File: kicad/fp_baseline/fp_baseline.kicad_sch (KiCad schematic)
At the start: 1 part, among them J1 JS220

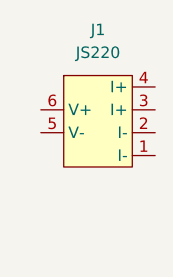
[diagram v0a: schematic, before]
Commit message: fix front copper polygon so it acts as prper copper pour around pads
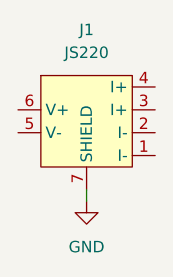
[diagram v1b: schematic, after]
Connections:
- new net GND: J1.7 (SHIELD)
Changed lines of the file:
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@@
 (kicad_sch (version 20211123) (generator eeschema)
   (paper "A4")
-  (symbol (lib_id "Joulescope:JS220") (at 140.97 100.33 0) (unit 1)
+  (wire (pts (xy 139.7 107.95) (xy 139.7 109.22))
+    (stroke (width 0) (type default) (color 0 0 0 0))
+  )
+  (symbol (lib_id "power:GND") (at 139.7 109.22 0) (unit 1)
     (in_bom yes) (on_board yes) (fields_autoplaced)
-    (property "Reference" "J1" (id 0) (at 140.97 90.17 0))
-    (property "Value" "JS220" (id 1) (at 140.97 92.71 0))
-    (property "Footprint" "Joulescope:JS220" (id 2) (at 140.97 100.33 0)
+    (property "Reference" "#PWR0101" (id 0) (at 139.7 115.57 0)
       (effects (font (size 1.27 1.27)) hide)
     )
-    (property "Datasheet" "" (id 3) (at 140.97 100.33 0)
+    (property "Value" "GND" (id 1) (at 139.7 114.3 0))
+    (property "Footprint" "" (id 2) (at 139.7 109.22 0)
+      (effects (font (size 1.27 1.27)) hide)
+    )
+    (property "Datasheet" "" (id 3) (at 139.7 109.22 0)
+      (effects (font (size 1.27 1.27)) hide)
+    )
+    (pin "1")
+  )
+  (symbol (lib_id "Joulescope:JS220") (at 139.7 100.33 0) (unit 1)
+    (in_bom yes) (on_board yes) (fields_autoplaced)
+    (property "Reference" "J1" (id 0) (at 139.7 90.17 0))
+    (property "Value" "JS220" (id 1) (at 139.7 92.71 0))
+    (property "Footprint" "Joulescope:JS220" (id 2) (at 139.7 100.33 0)
+      (effects (font (size 1.27 1.27)) hide)
+    )
+    (property "Datasheet" "" (id 3) (at 139.7 100.33 0)
       (effects (font (size 1.27 1.27)) hide)
     )
@@
     (pin "5")
     (pin "6")
+    (pin "7")
   )
   (sheet_instances
@@
   )
   (symbol_instances
+    (path "/371c245b-12ff-418c-ad6a-38bf35510b4d"
+      (reference "#PWR0101") (unit 1) (value "GND") (footprint "")
+    )
     (path "/376cee22-538a-400e-85e1-282bd8cf6c38"
       (reference "J1") (unit 1) (value "JS220") (footprint "Joulescope:JS220")
